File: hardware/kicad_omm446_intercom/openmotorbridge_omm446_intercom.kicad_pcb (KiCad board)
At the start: 4 copper layers, 60 x 30 mm, 22 parts, among them J1 TYPE-C-31-M-12_IP67, SW1 BTN_PTT, SW2 BTN_MODE, SW3 BTN_CH_UP, SW4 BTN_CH_DOWN, U1 ESP32-C6-MINI-1U, U2 BQ24075RGTR, U3 SA818-DMR, U4 ES8388, U5 ME6211C33M5G, U6 ESP32-PICO-V3-02

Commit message: fix(hw): place J_HELMET on F.Cu top side facing right edge on PCBA 09 and 10
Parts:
- J_HELMET: moved to F.Cu

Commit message: fix(omm446): correct NiceRF SA818 VRML scale factor and synchronize 3D PCBA renders
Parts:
- turned J_HELMET to -90 degrees
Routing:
- net VCC_3V3: track 97.6 -> 78.4 mm
- net BTN_PTT: track 54.3 -> 69.2 mm, vias 6 -> 5
- net GND: track 24.1 -> 9.83 mm, vias 7 -> 5
- net HP_OUT_L: track 56.1 -> 66.9 mm, vias 3 -> 2
- net WS2812_DATA: track 30.6 -> 20.5 mm
- net AGND_SPK: track 61.1 -> 70.3 mm, vias 2 -> 6
- net BTN_MODE: track 10.3 -> 18.3 mm
- net HP_OUT_R: track 47.6 -> 54.8 mm, vias 2 -> 3
- net VBUS_5V: track 45.9 -> 49.1 mm, vias 4 -> 5
- net BTN_CH_DOWN: track 32.6 -> 30.1 mm, vias 3 -> 2
- net USB_DN: track 19.9 -> 18.5 mm, vias 6 -> 2
- net I2C_SDA: track 8.28 -> 7.19 mm
- net I2S_DOUT: track 12.4 -> 11.3 mm
- net MIC_IN+: track 61.2 -> 60.5 mm, vias 6 -> 0
- net CHG_STAT: track 24.0 -> 23.4 mm
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
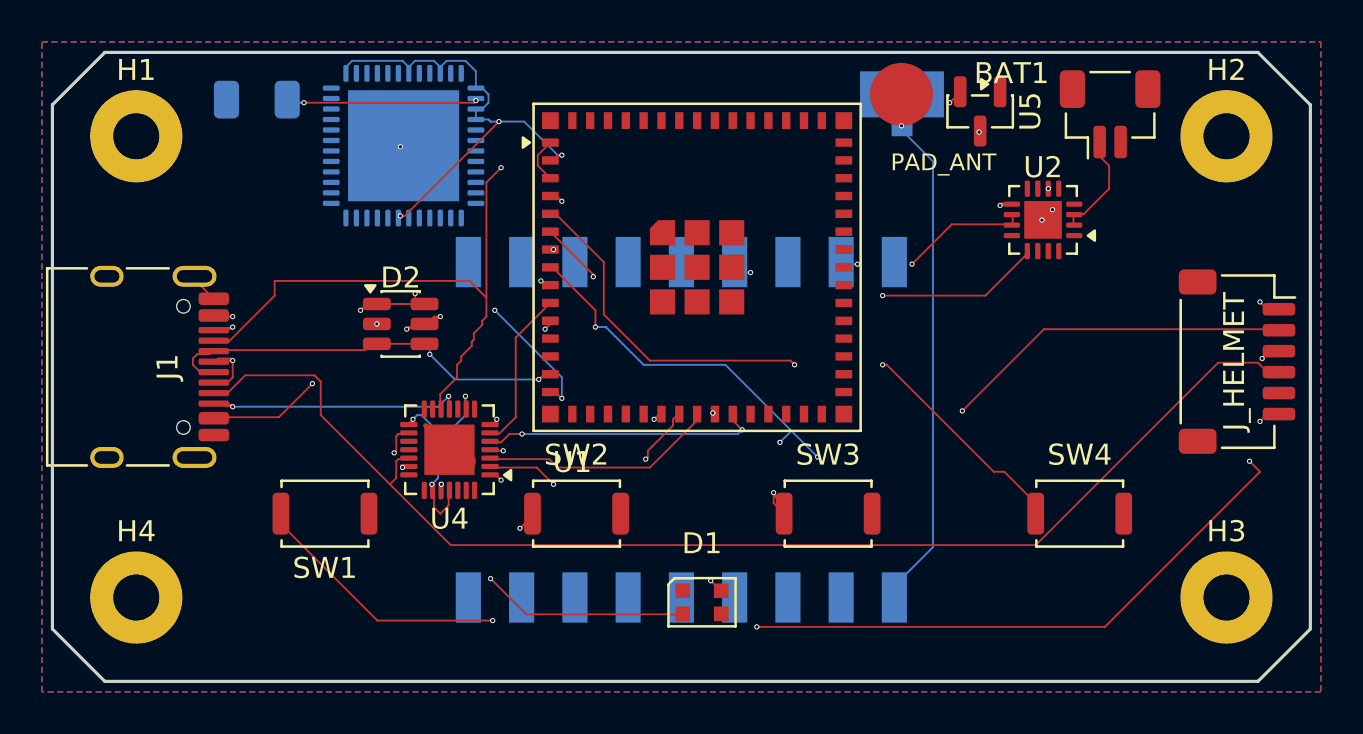
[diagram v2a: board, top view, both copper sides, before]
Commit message: fix(hardware): fleet-wide 7-PCBA remediation, schematic parity & doc alignment
- PCBA 01 (Central Box): Synchronized DTM-12 schematic and PCB routing, purged obsolete analog audio transformers/HD26 connector.
- PCBA 03 (Smart Cartridge): Verified Kelvin ground isolation on J_AUDIO_PWR, resolved U1.16 BAY_SELECT single net.
- PCBA 05 (Front Node): Mapped DW3110 UWB SPI/IRQ/RST to ESP32-S3 pads 30-35, connected MK1 I2S MEMS mic and Y_UWB crystal.
- PCBA 07 (Smart Keyfob): Connected 12 unrouted signals (SX1262 LoRa SPI, DRV2605L I2C, SWD, RTC crystal, buttons) to nRF52840 pads.
- PCBA 08 (Radar Sub-MCU): Synchronized J1.1 power rail to VCC_5V, connected Y1_UWB crystal to DW3110 pads 4 & 5.
- PCBA 09 & PCBA 10 (OMM 2.4 GHz & 446 MHz): Verified 4-layer stackup, BQ24075 ground ties, SA818 isolation, and vertical B.Cu J_HELMET orientation.
- Tools: Added verify_hardware_integrity.py with automated DRC/parity/single-net/floating-pad checks (all 7 PCBAs HEALTHY).
- Docs: Synchronized docs/de and docs/en hardware specifications, pinouts, and DTM-12 architecture.
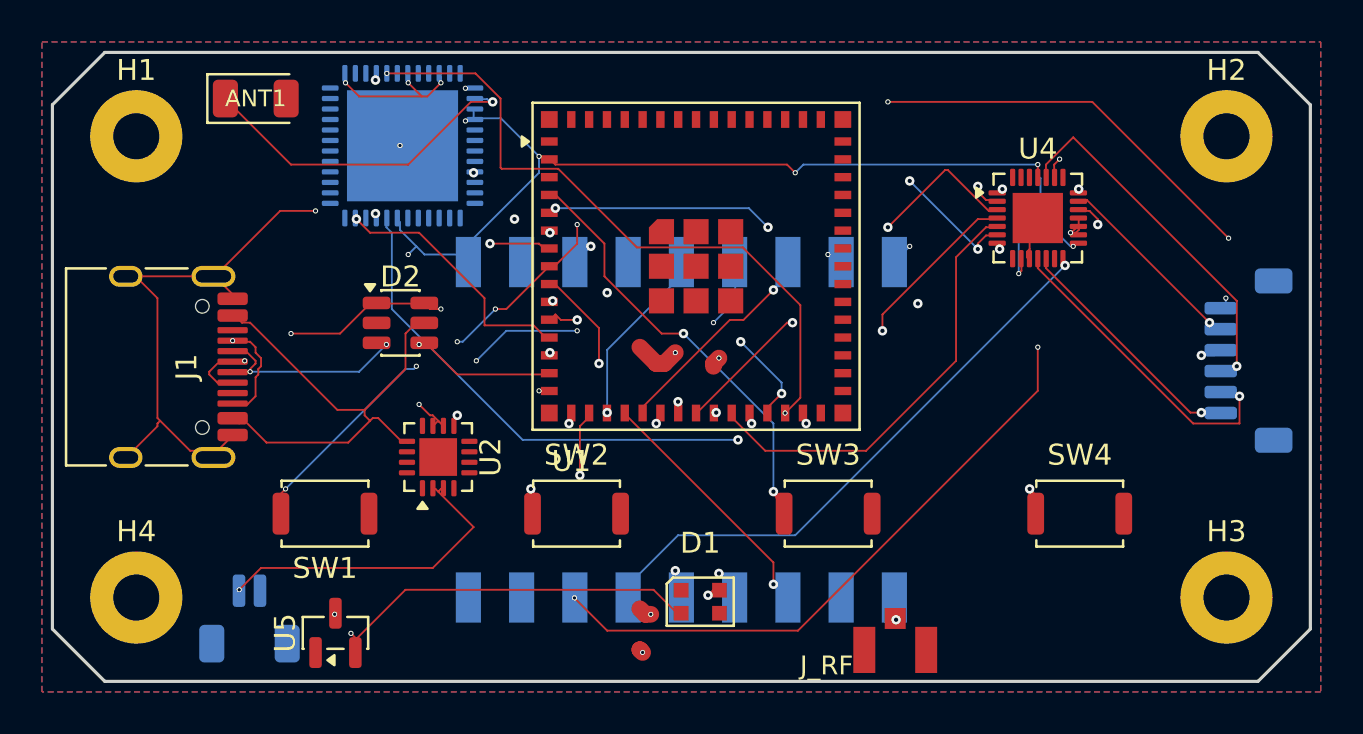
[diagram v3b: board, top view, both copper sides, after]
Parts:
- removed the J_HELMET at (126.5, 99.8)
- removed PAD_ANT: Contact_Spring_Helix, TestPoint_Pad_D3.0mm
- added J_HELMET: HELMET_AUDIO_6P, JST_SH_BM06B-SRSS-TB_1x06-1MP_P1.00mm_Vertical, B.Cu at (127.0, 99.7)
- ANT1, J_RF: moved to F.Cu
- BAT1: moved to B.Cu
- moved BAT1 47.6 mm to (79.4, 112.0)
- moved U5 39.6 mm to (83.5, 112.7), turned to 90 degrees
- moved U2 31.0 mm to (88.4, 104.3), turned to 90 degrees
- moved U4 30.2 mm to (117.0, 92.9), turned to 0 degrees
- moved J_RF 26.5 mm to (110.2, 113.5)
- moved J1 0.90 mm to (74.5, 100.0)
- moved D1 0.09 mm to (100.9, 111.2)
- moved ANT1 0.07 mm to (79.7, 87.2), turned to 180 degrees
- moved U1 0.07 mm to (100.7, 95.2)
- moved D2 0.05 mm to (86.6, 97.9)
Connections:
- net BTN_CH_DOWN renamed BTN_4
- net BTN_CH_UP renamed BTN_3
- net BTN_MODE renamed BTN_2
- net BTN_PTT renamed BTN_1
- D1 pad 1: (no net) -> GND
- J1 pad A1: GND -> PGND
- J1 pad A12: GND -> PGND
- J1 pad A5: HP_OUT_L -> GND
- J1 pad A8: MIC_IN+ -> (no net)
- J1 pad B1: GND -> PGND
- J1 pad B12: GND -> PGND
- J1 pad B5: HP_OUT_R -> GND
- J1 pad B8: AGND_SPK -> (no net)
- J1 pad SH: GND -> PGND
- U1 pad 12: (no net) -> BT_BOOT
- U1 pad 13: (no net) -> BT_RESET
- U1 pad 16: (no net) -> SA818_TXD
- U1 pad 17: (no net) -> SA818_RXD
- U1 pad 18: (no net) -> SA818_PTT
- U1 pad 19: (no net) -> SA818_SQL
- U1 pad 20: (no net) -> SA818_PWR_HL
- U1 pad 26: (no net) -> BT_UART_CTS
- U1 pad 27: (no net) -> BT_UART_RTS
- U1 pad 28: (no net) -> BT_UART_TX
- U1 pad 29: (no net) -> BT_UART_RX
- U1 pad 54: (no net) -> GND
- U1 pad 55: (no net) -> GND
- U1 pad 56: (no net) -> GND
- U1 pad 57: (no net) -> GND
- U1 pad 58: (no net) -> GND
- U1 pad 59: (no net) -> GND
- U1 pad 60: (no net) -> GND
- U1 pad 61: (no net) -> GND
- U1 pad 62: (no net) -> GND
- U1 pad 63: (no net) -> GND
- U1 pad 64: (no net) -> GND
- U1 pad 65: (no net) -> GND
- U2 pad 1: NTC_TS -> GND
- U2 pad 12: ILIM -> GND
- U2 pad 16: ISET -> GND
- U2 pad 6: SYS_PWR -> GND
- U3 pad 1: AUDIO_ON -> VCC_3V3
- U4 pad 11: HP_OUT_R -> AUDIO_OUT_R
- U4 pad 12: HP_OUT_L -> AUDIO_OUT_L
- U4 pad 14: (no net) -> SA818_MIC_IN
- U4 pad 16: AGND_SPK -> AGND
- U4 pad 17: VREF -> AGND
- U4 pad 18: MICBIAS -> AGND
- U4 pad 19: MIC_IN+ -> VOICE_IN
- U4 pad 20: AGND_SPK -> AGND_MIC
- U4 pad 21: (no net) -> SA818_AF_OUT
- U4 pad 24: GND -> AGND_SPK
- U6 pad : (no net) -> GND
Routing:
- net HP_OUT_L: track 66.9 -> 0.00 mm, vias 2 -> 0
- net PGND: track 0.00 -> 62.8 mm, vias 0 -> 2
- net MIC_IN+: track 60.5 -> 0.00 mm
- net HP_OUT_R: track 54.8 -> 0.00 mm, vias 3 -> 0
- net BT_UART_RX: track 0.00 -> 53.1 mm, vias 0 -> 2
- net AGND_SPK: track 70.3 -> 17.6 mm, vias 6 -> 1
- net AGND: track 0.00 -> 37.4 mm, vias 0 -> 3
- net BT_UART_TX: track 0.00 -> 31.7 mm, vias 0 -> 2
- net I2C_SCL: track 6.10 -> 35.5 mm
- net SA818_MIC_IN: track 0.00 -> 28.2 mm, vias 0 -> 1
- net SA818_AF_OUT: track 0.00 -> 27.9 mm, vias 0 -> 2
- net BT_UART_CTS: track 0.00 -> 25.2 mm, vias 0 -> 2
- net VBUS_5V: track 49.1 -> 23.9 mm, vias 5 -> 0
- net BT_UART_RTS: track 0.00 -> 24.8 mm, vias 0 -> 5
- net RF_ANT: track 24.6 -> 1.15 mm
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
